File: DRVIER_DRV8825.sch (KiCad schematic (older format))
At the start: 23 parts, among them P7 CONN_01X05, P8 CONN_01X03, P9 CONN_02X08, U5 DRV8825

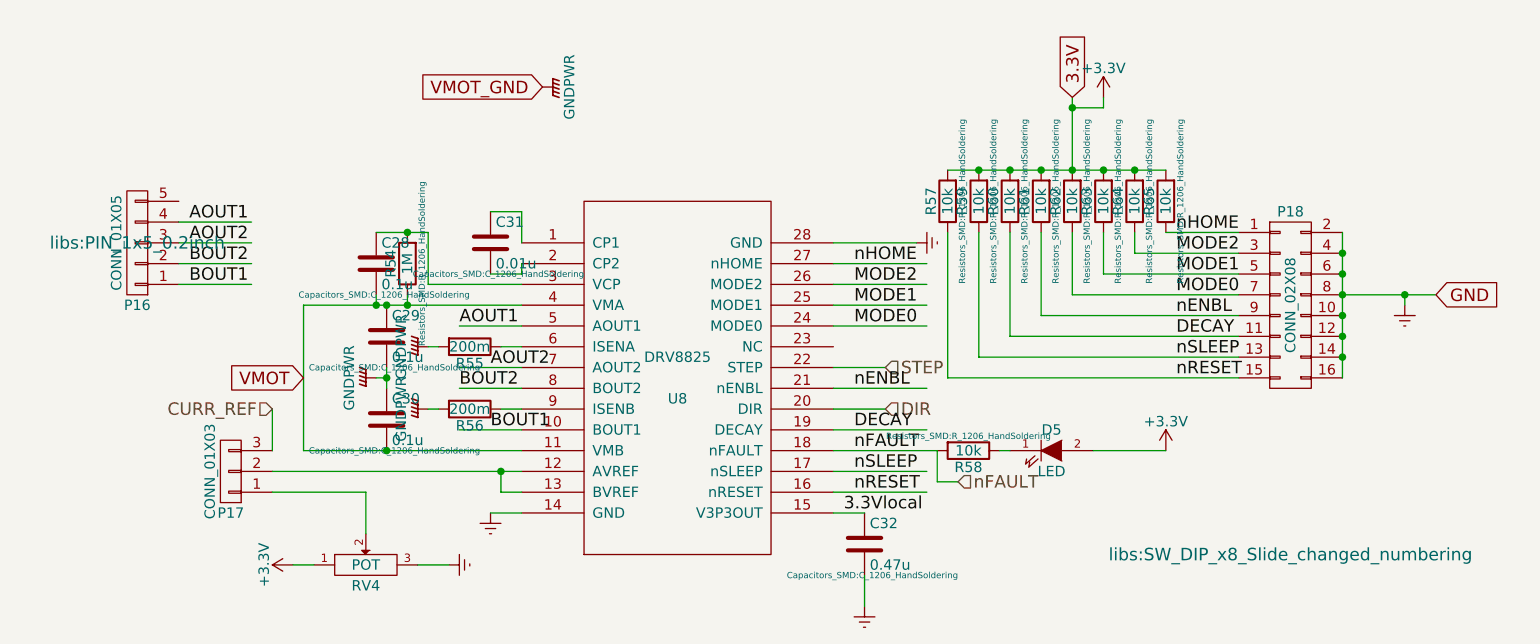
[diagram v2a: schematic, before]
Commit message: minor changes in layout
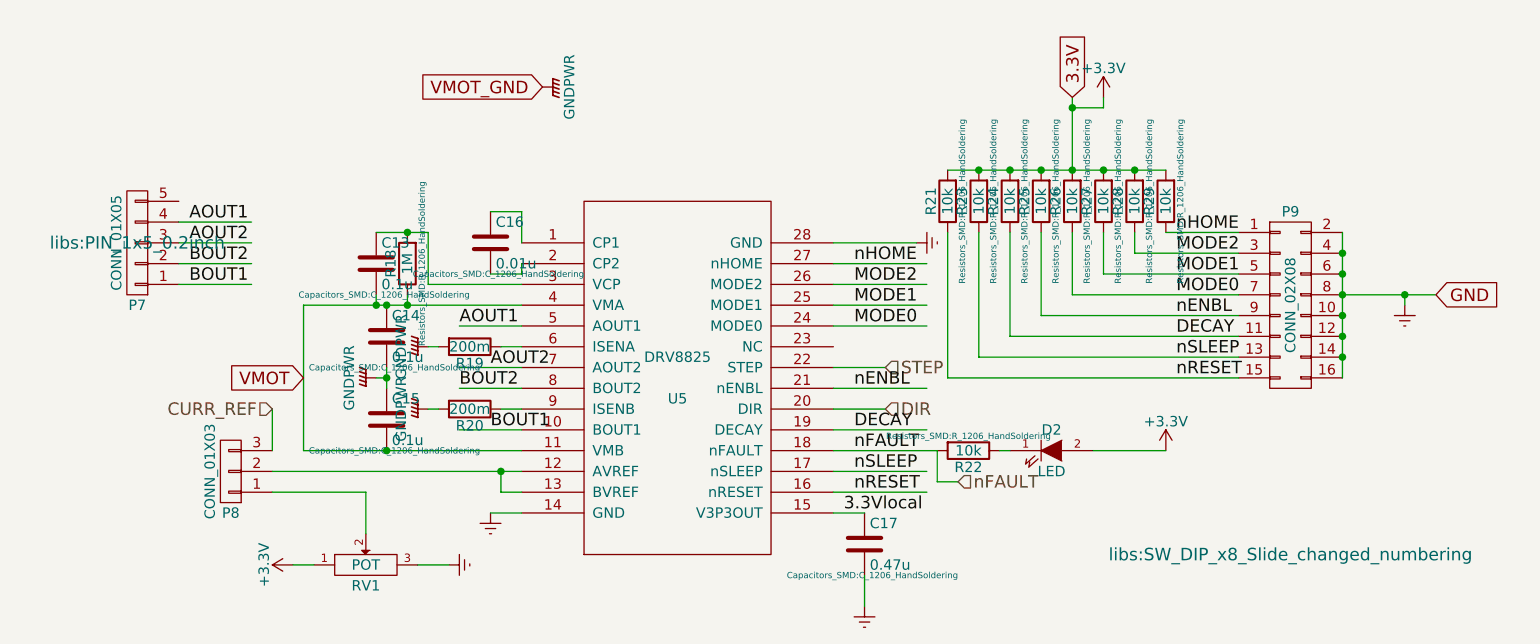
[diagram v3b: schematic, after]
